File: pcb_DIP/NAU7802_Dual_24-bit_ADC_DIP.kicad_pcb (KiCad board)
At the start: 2 copper layers, 50.8 x 22.9 mm, 34 parts, among them J1 CELL_A, J2 CELL_B, J3 STEMMA_QT, J4 STEMMA_QT, M1 Feather_M4_Express, U1 NAU7802

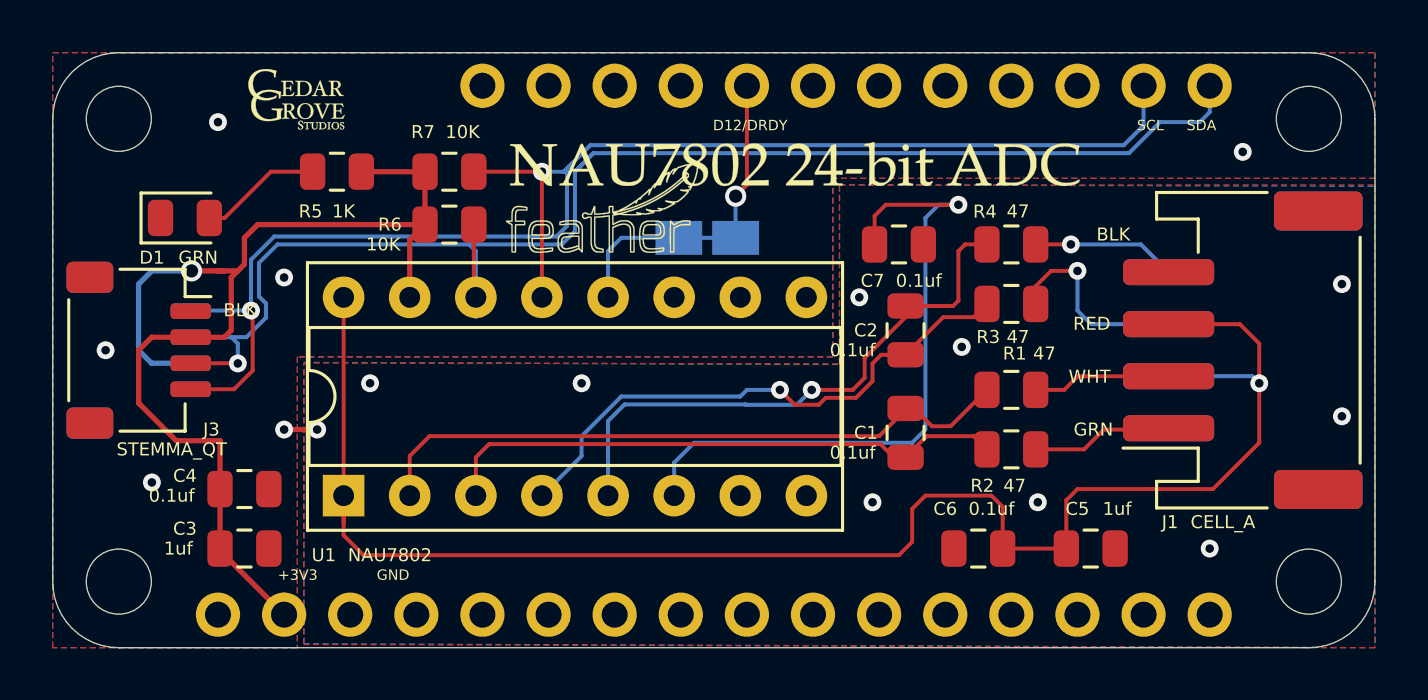
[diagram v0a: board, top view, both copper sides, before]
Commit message: refactor wing for NAU7802 ADC DIP package
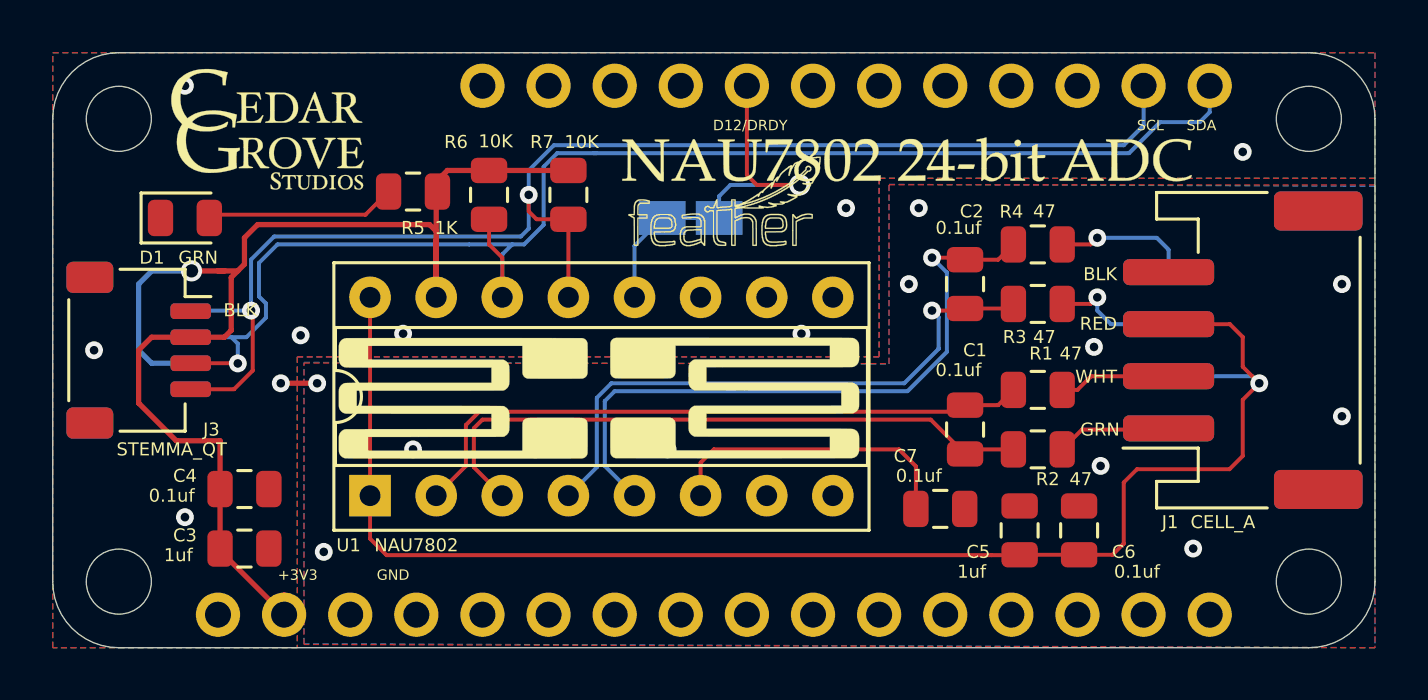
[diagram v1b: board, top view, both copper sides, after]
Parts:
- removed the G*** at (137.7, 91.9)
- added G***: NAU7802_STRAIN_LOGO_10x5mm, Adafruit:NAU7802_STRAIN_LOGO_10x5mm, F.Cu at (154.4, 103.4)
- added G***: LOGO, Adafruit:CedarGroveStudios_TEXT_LOGO_8x5_4mm, F.Cu at (136.6, 93.1)
- G***: moved to F.Cu
- moved G*** 25.0 mm to (138.4, 93.5)
- moved G*** 11.4 mm to (144.1, 103.4), turned to 180 degrees
- moved C7 10.3 mm to (162.4, 107.7)
- moved G*** 4.71 mm to (154.1, 95.8)
- moved R7 4.66 mm to (148.1, 95.6), turned to 90 degrees
- moved G*** 4.31 mm to (161.1, 94.3)
- moved R5 3.02 mm to (142.1, 95.5)
- moved C2 2.90 mm to (163.3, 99.1)
- moved C1 2.29 mm to (163.3, 104.6)
- moved R6 1.91 mm to (145.0, 95.6), turned to 90 degrees
- moved C6 1.73 mm to (165.4, 108.5), turned to 90 degrees
- moved R1 1.02 mm to (166.1, 103.1)
- moved R2 1.02 mm to (166.1, 105.4)
- moved R3 1.02 mm to (166.1, 99.8)
- moved R4 1.02 mm to (166.1, 97.5)
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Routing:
- net Net-(C7-Pad1): track 25.6 -> 11.7 mm, vias 1 -> 0
- net +3V3: track 45.5 -> 50.7 mm
- net /AVDD: track 63.4 -> 58.2 mm
- net /SCL: track 57.9 -> 53.9 mm
- net /B+: track 22.1 -> 25.3 mm
- net /CELL_B-: track 7.77 -> 4.92 mm
- net Net-(D1-Pad2): track 4.70 -> 7.31 mm
- net /A+: track 22.1 -> 24.5 mm
- net /DRDY: track 13.6 -> 16.0 mm
- net /SDA: track 56.3 -> 55.1 mm
- net /CELL_A-: track 5.32 -> 4.30 mm
- net /B-: track 22.2 -> 22.9 mm
- net /CELL_A+: track 5.19 -> 4.50 mm
- net /A-: track 25.4 -> 24.8 mm
- net GND: track 1.27 -> 1.40 mm, vias 16 -> 21
